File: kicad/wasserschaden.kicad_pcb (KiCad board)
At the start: 2 copper layers, 50.8 x 50.2 mm, 16 parts, among them J1 valve out, J2 12V in, U2 WeMos_mini

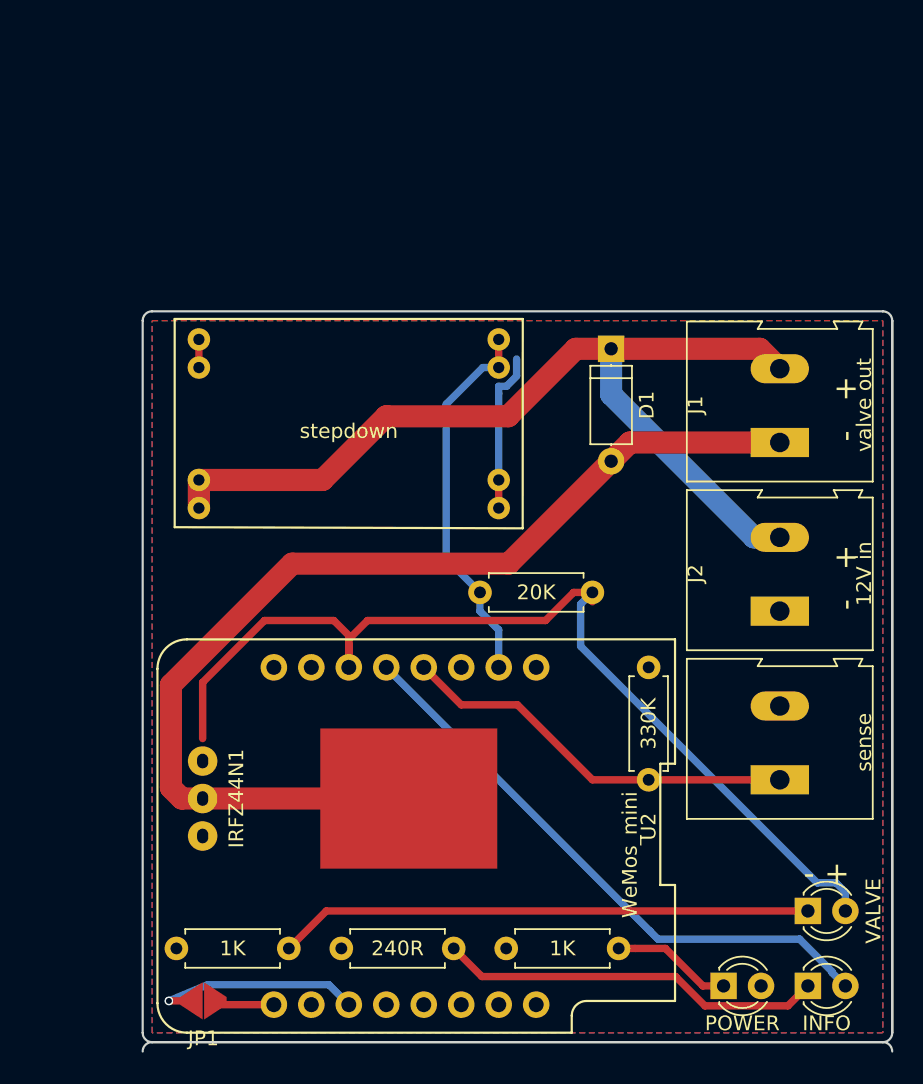
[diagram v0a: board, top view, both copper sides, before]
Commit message: major pcb rearangement
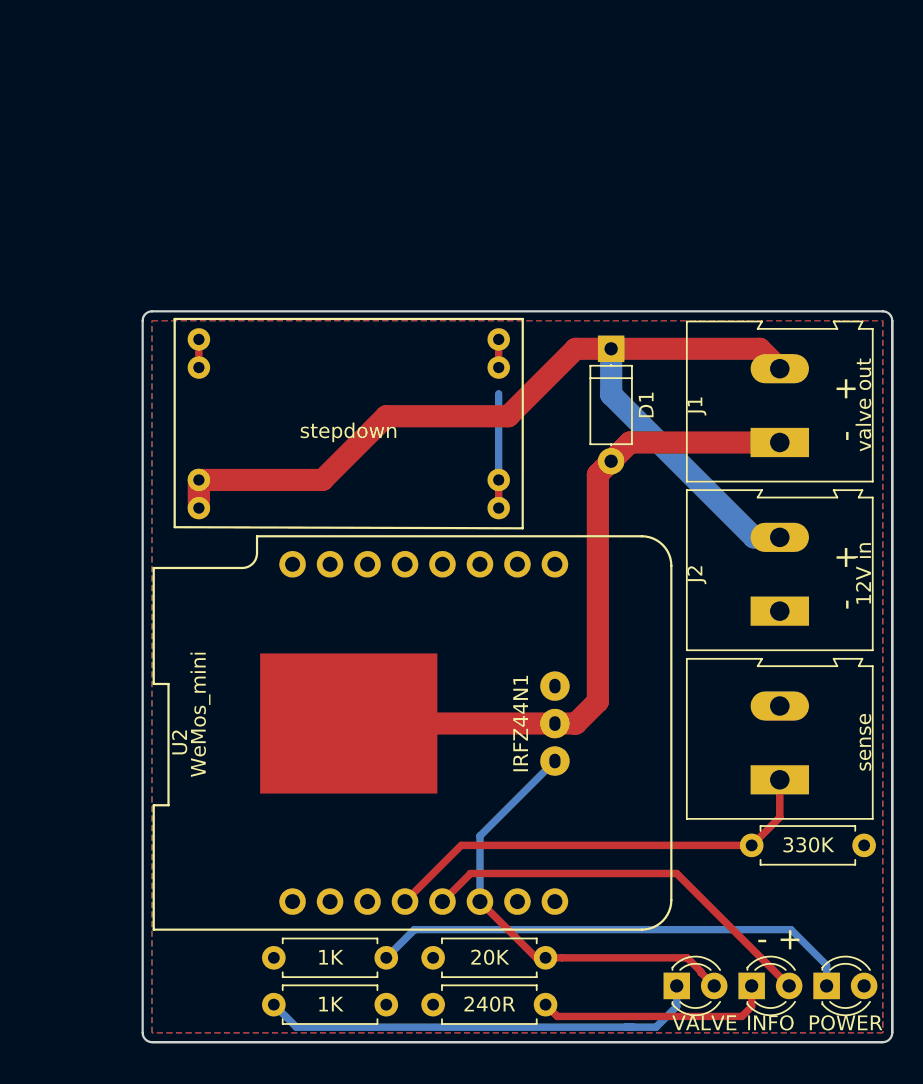
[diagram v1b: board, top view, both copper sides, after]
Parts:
- removed JP1: deepsleep jumper, custom:jumper
- moved 20K 25.0 mm to (145.4, 102.2)
- moved 1K 15.8 mm to (142.2, 102.2)
- moved 1K 14.7 mm to (142.2, 105.4), turned to 180 degrees
- moved IRFZ44N1 14.2 mm to (148.3, 86.4), turned to 0 degrees
- moved VALVE 10.2 mm to (161.9, 104.1)
- moved 330K 8.28 mm to (167.0, 94.6), turned to 0 degrees
- moved 240R 7.30 mm to (145.4, 105.4)
- moved U2 7.10 mm to (144.8, 87.0), turned to 0 degrees
- moved POWER 6.99 mm to (172.1, 104.1)
- moved INFO 3.81 mm to (167.0, 104.1)
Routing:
- net Net-(D2-Pad2): track 68.3 -> 30.5 mm
- net Net-(D1-Pad2): track 71.5 -> 46.1 mm
- net Net-(D3-Pad1): track 8.16 -> 33.0 mm
- net GND: track 27.7 -> 3.81 mm
- net Net-(JP1-Pad1): track 14.5 -> 0.00 mm, vias 1 -> 0
- net Net-(D4-Pad2): track 40.1 -> 27.4 mm
- net Net-(D4-Pad1): track 26.2 -> 16.0 mm
- net Net-(D2-Pad1): track 36.2 -> 30.4 mm
- net Net-(JP1-Pad2): track 4.07 -> 0.00 mm
- net +3V3: track 10.9 -> 7.75 mm
- net Net-(J3-Pad1): track 27.3 -> 30.3 mm
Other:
- board size 50.8 x 50.2 mm -> 50.8 x 49.5 mm

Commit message: pcb redesigen
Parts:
- added JP1: deepsleep jumper, custom:jumper, F.Cu at (151.1, 80.0)
- renumbered VALVE to D2, POWER to D3, INFO to D4, sense to J3, 20K to R1, 1K to R2, 1K to R3, 240R to R4, 330K to R5, stepdown to U1
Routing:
- net Net-(JP1-Pad1): track 0.00 -> 5.16 mm
- net Net-(JP1-Pad2): track 0.00 -> 5.16 mm
- added copper zone on F.Cu, net +3V3
- added copper zone on B.Cu, net GND
- removed copper zone on B.Cu, net +3V3
- removed copper zone on F.Cu, net GND
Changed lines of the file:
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@@
     (thickness 1.6)
     (drawings 13)
-    (tracks 54)
+    (tracks 58)
     (zones 0)
-    (modules 15)
+    (modules 16)
     (nets 22)
   )
@@
     (visible_elements FFFFFFFF)
     (pcbplotparams
-      (layerselection 0x010f0_80000001)
+      (layerselection 0x010f0_ffffffff)
       (usegerberextensions false)
       (usegerberattributes false)
@@
   (module custom:stepdown (layer F.Cu)
     (at 139.7 66.04)
-    (fp_text reference stepdown (at 0 0.5) (layer F.SilkS)
+    (fp_text reference U1 (at 0 0.5) (layer F.SilkS)
       (effects (font (size 1 1) (thickness 0.15)))
     )
@@
     (descr "Resistor, Axial_DIN0207 series, Axial, Horizontal, pin pitch=7.62mm, 0.25W = 1/4W, length*diameter=6.3*2.5mm^2, http://cdn-reichelt.de/documents/datenblatt/B400/1_4W%23YAG.pdf")
     (tags "Resistor Axial_DIN0207 series Axial Horizontal pin pitch 7.62mm 0.25W = 1/4W length 6.3mm diameter 2.5mm")
-    (fp_text reference 1K (at 3.81 0) (layer F.SilkS)
+    (fp_text reference R3 (at 3.81 0) (layer F.SilkS)
       (effects (font (size 1 1) (thickness 0.15)))
     )
@@
     (descr "LED, diameter 3.0mm, 2 pins")
     (tags "LED diameter 3.0mm 2 pins")
-    (fp_text reference INFO (at 1.27 2.54) (layer F.SilkS)
+    (fp_text reference D4 (at 1.27 2.54) (layer F.SilkS)
       (effects (font (size 1 1) (thickness 0.15)))
     )
@@
     (descr "LED, diameter 3.0mm, 2 pins")
     (tags "LED diameter 3.0mm 2 pins")
-    (fp_text reference POWER (at 1.27 2.54) (layer F.SilkS)
+    (fp_text reference D3 (at 1.27 2.54) (layer F.SilkS)
       (effects (font (size 1 1) (thickness 0.15)))
     )
@@
     (descr "LED, diameter 3.0mm, 2 pins")
     (tags "LED diameter 3.0mm 2 pins")
-    (fp_text reference VALVE (at 1.905 2.54 180) (layer F.SilkS)
+    (fp_text reference D2 (at 1.905 2.54 180) (layer F.SilkS)
       (effects (font (size 1 1) (thickness 0.15)))
     )
@@
     (descr "Resistor, Axial_DIN0207 series, Axial, Horizontal, pin pitch=7.62mm, 0.25W = 1/4W, length*diameter=6.3*2.5mm^2, http://cdn-reichelt.de/documents/datenblatt/B400/1_4W%23YAG.pdf")
     (tags "Resistor Axial_DIN0207 series Axial Horizontal pin pitch 7.62mm 0.25W = 1/4W length 6.3mm diameter 2.5mm")
-    (fp_text reference 20K (at 3.81 0) (layer F.SilkS)
+    (fp_text reference R1 (at 3.81 0) (layer F.SilkS)
       (effects (font (size 1 1) (thickness 0.15)))
     )
@@
     (descr "Resistor, Axial_DIN0207 series, Axial, Horizontal, pin pitch=7.62mm, 0.25W = 1/4W, length*diameter=6.3*2.5mm^2, http://cdn-reichelt.de/documents/datenblatt/B400/1_4W%23YAG.pdf")
     (tags "Resistor Axial_DIN0207 series Axial Horizontal pin pitch 7.62mm 0.25W = 1/4W length 6.3mm diameter 2.5mm")
-    (fp_text reference 1K (at 3.81 0 180) (layer F.SilkS)
+    (fp_text reference R2 (at 3.81 0 180) (layer F.SilkS)
       (effects (font (size 1 1) (thickness 0.15)))
     )
@@
     (descr "Resistor, Axial_DIN0207 series, Axial, Horizontal, pin pitch=7.62mm, 0.25W = 1/4W, length*diameter=6.3*2.5mm^2, http://cdn-reichelt.de/documents/datenblatt/B400/1_4W%23YAG.pdf")
     (tags "Resistor Axial_DIN0207 series Axial Horizontal pin pitch 7.62mm 0.25W = 1/4W length 6.3mm diameter 2.5mm")
-    (fp_text reference 240R (at 3.81 0) (layer F.SilkS)
+    (fp_text reference R4 (at 3.81 0) (layer F.SilkS)
       (effects (font (size 1 1) (thickness 0.15)))
     )
@@
     (descr "Altech AK300 terminal block, pitch 5.0mm, 45 degree angled, see http://www.mouser.com/ds/2/16/PCBMETRC-24178.pdf")
     (tags "Altech AK300 terminal block pitch 5.0mm")
-    (fp_text reference sense (at 2.54 5.715 90) (layer F.SilkS)
+    (fp_text reference J3 (at 2.54 5.715 90) (layer F.SilkS)
       (effects (font (size 1 1) (thickness 0.15)))
     )
@@
     (descr "Resistor, Axial_DIN0207 series, Axial, Horizontal, pin pitch=7.62mm, 0.25W = 1/4W, length*diameter=6.3*2.5mm^2, http://cdn-reichelt.de/documents/datenblatt/B400/1_4W%23YAG.pdf")
     (tags "Resistor Axial_DIN0207 series Axial Horizontal pin pitch 7.62mm 0.25W = 1/4W length 6.3mm diameter 2.5mm")
-    (fp_text reference 330K (at 3.81 0 180) (layer F.SilkS)
+    (fp_text reference R5 (at 3.81 0 180) (layer F.SilkS)
       (effects (font (size 1 1) (thickness 0.15)))
     )
@@
     )
   )
+  (module custom:jumper (layer F.Cu)
+    (at 151.13 80.01)
+    (fp_text reference JP1 (at 0 2.54) (layer F.SilkS)
+      (effects (font (size 1 1) (thickness 0.15)))
+    )
+    (fp_text value "deepsleep jumper" (at 0 1.27) (layer F.Fab)
+      (effects (font (size 1 1) (thickness 0.15)))
+    )
+    (pad 1 smd trapezoid (at -0.8128 0) (size 1.524 1.524) (rect_delta -1 0 ) (layers F.Cu F.Paste F.Mask)
+      (net 19 "Net-(JP1-Pad1)"))
+    (pad 2 smd trapezoid (at 0.8128 0) (size 1.524 1.524) (rect_delta 1 0 ) (layers F.Cu F.Paste F.Mask)
+      (net 20 "Net-(JP1-Pad2)"))
+  )
   (gr_arc (start 175.895 107.315) (end 176.53 107.315) (angle 90) (layer Edge.Cuts) (width 0.15))
   (gr_text "- +" (at 168.91 100.965) (layer F.SilkS)
@@
   (segment (start 149.86 69.85) (end 149.86 71.755) (width 0.5) (layer F.Cu) (net 18))
   (segment (start 149.86 69.85) (end 149.86 64.008) (width 0.5) (layer B.Cu) (net 18))
+  (segment (start 148.59 75.565) (end 148.59 78.2828) (width 0.5) (layer F.Cu) (net 19))
+  (segment (start 150.3172 80.01) (end 148.59 78.2828) (width 0.5) (layer F.Cu) (net 19))
+  (segment (start 153.67 78.2828) (end 153.67 75.565) (width 0.5) (layer F.Cu) (net 20))
+  (segment (start 151.9428 80.01) (end 153.67 78.2828) (width 0.5) (layer F.Cu) (net 20))
   (segment (start 147.32 94.615) (end 167.005 94.615) (width 0.5) (layer F.Cu) (net 21))
   (segment (start 143.51 98.425) (end 147.32 94.615) (width 0.5) (layer F.Cu) (net 21))
   (segment (start 168.91 92.71) (end 167.005 94.615) (width 0.5) (layer F.Cu) (net 21))
   (segment (start 168.91 90.17) (end 168.91 92.71) (width 0.5) (layer F.Cu) (net 21))
-  (zone (net 3) (net_name GND) (layer F.Cu) (hatch edge 0.508)
+  (zone (net 18) (net_name +3V3) (layer F.Cu) (hatch edge 0.508)
     (connect_pads (clearance 0.508))
     (min_thickness 0.254)
@@
     )
   )
-  (zone (net 18) (net_name +3V3) (layer B.Cu) (hatch edge 0.508)
+  (zone (net 3) (net_name GND) (layer B.Cu) (hatch edge 0.508)
     (connect_pads (clearance 0.508))
     (min_thickness 0.254)

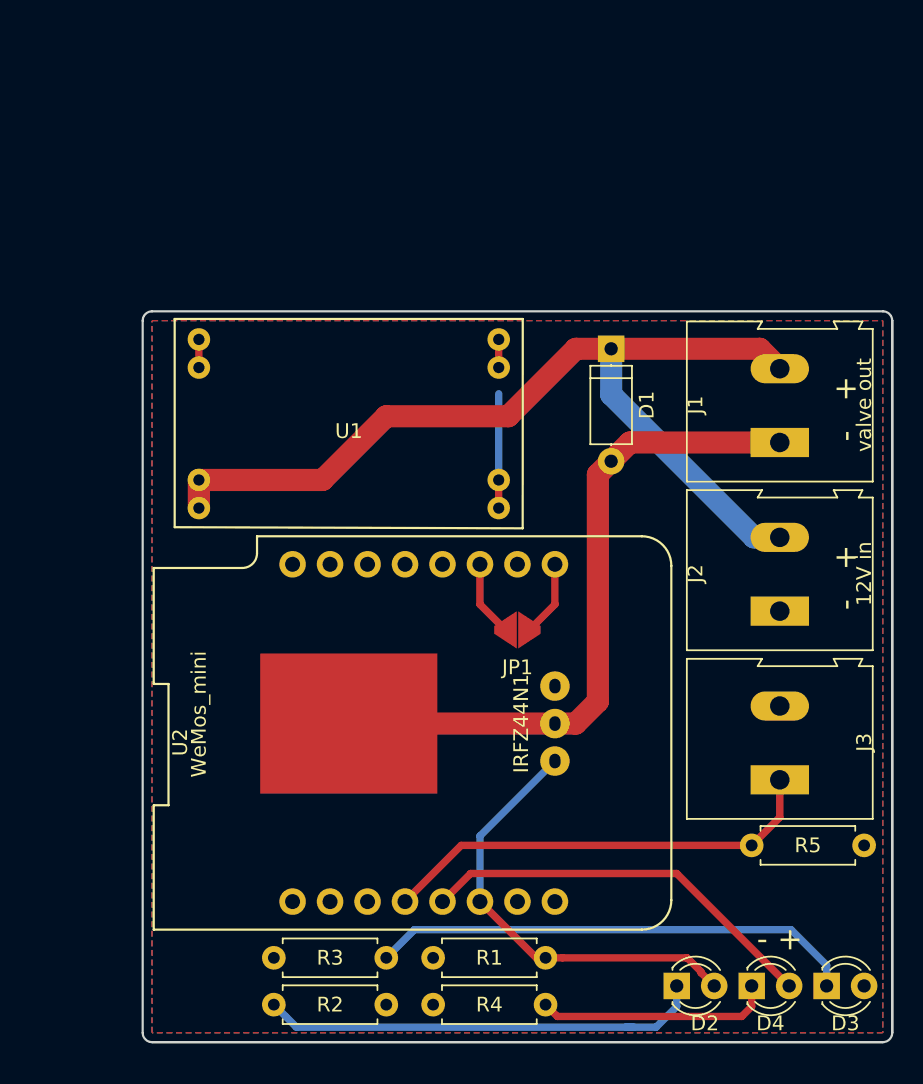
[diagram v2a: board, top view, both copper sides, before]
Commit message: added temperature sensor
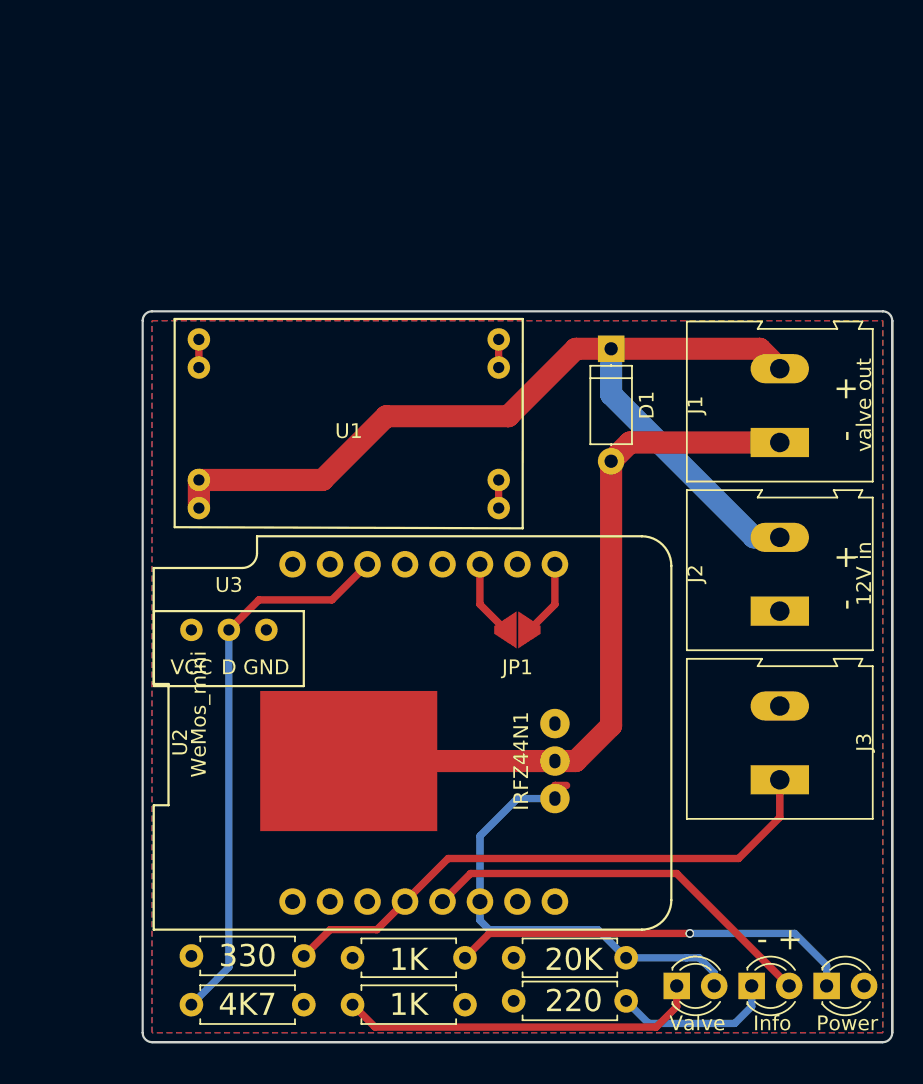
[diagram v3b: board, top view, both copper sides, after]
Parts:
- added R6: R, Resistors_THT:R_Axial_DIN0207_L6.3mm_D2.5mm_P7.62mm_Horizontal, F.Cu at (136.7, 105.4)
- added U3: DS18B20, custom:temperature_sensor, F.Cu at (131.6, 77.5)
- moved R5 31.3 mm to (136.7, 102.1), turned to 180 degrees
- moved R4 5.47 mm to (150.9, 105.2)
- moved R1 5.46 mm to (150.9, 102.2)
- moved R2 5.33 mm to (147.6, 105.4)
- moved R3 5.33 mm to (147.6, 102.2)
- moved IRFZ44N1 2.54 mm to (148.3, 88.9)
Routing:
- net Net-(R6-Pad2): track 0.00 -> 37.7 mm
- net Net-(J3-Pad1): track 30.3 -> 38.7 mm
- net +3V3: track 7.75 -> 1.91 mm
- net Net-(D2-Pad1): track 30.4 -> 24.6 mm
- net Net-(D3-Pad1): track 33.0 -> 27.5 mm, vias 0 -> 1
- net Net-(D4-Pad1): track 16.0 -> 11.0 mm
- net Net-(D1-Pad2): track 46.1 -> 48.7 mm
- net Net-(D2-Pad2): track 30.5 -> 32.4 mm
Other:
- board text added: "1K"
- board text added: "20K"
- board text added: "220"
- board text added: "330"
- board text added: "4K7"
- board text added: "Info"
- board text added: "Power"
- board text added: "Valve"

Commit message: added R values, improved stepdown footprint, rerouted resistors
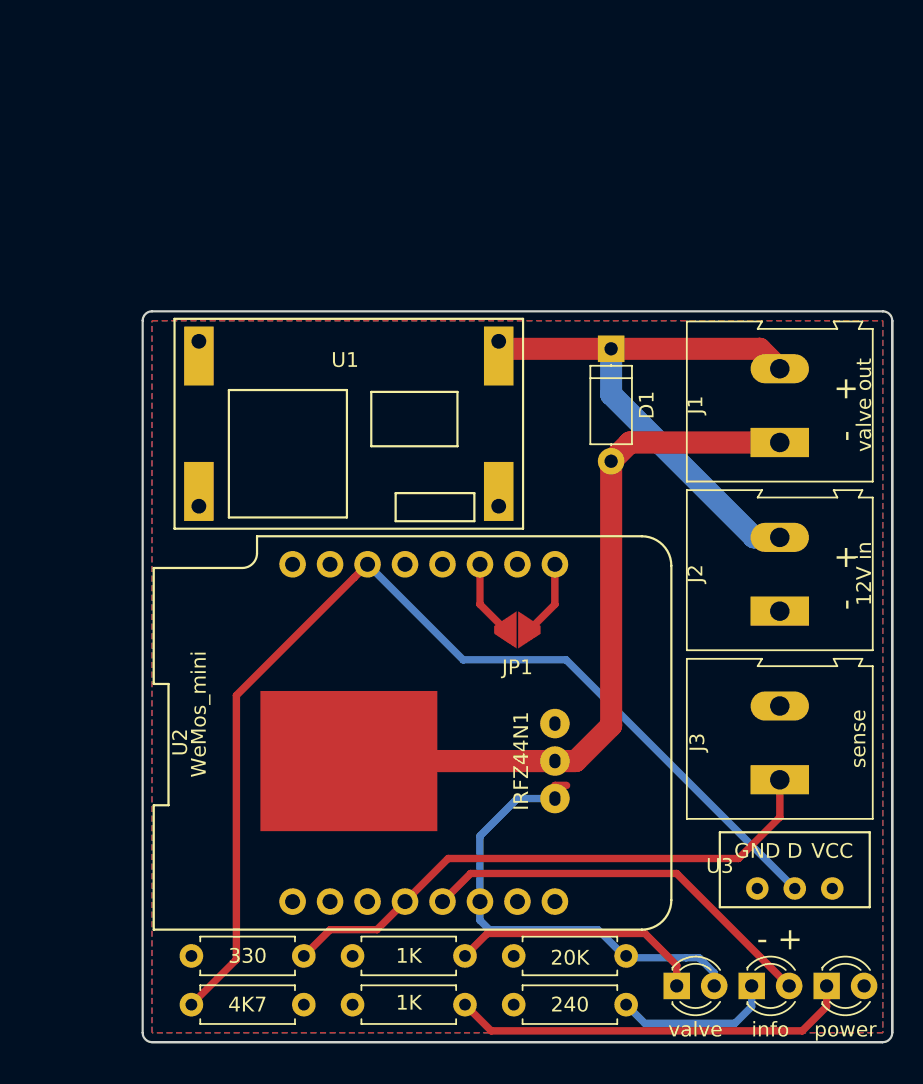
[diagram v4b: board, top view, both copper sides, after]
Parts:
- D2: value LED -> valve
- D3: value LED -> power
- D4: value LED -> info
- JP1: value deepsleep jumper -> deepsleep
- R2, R3: value R -> 1K
- R4: value R -> 240
- R5: value R -> 330
- R6: value R -> 4K7
- moved U3 44.5 mm to (169.9, 100.1), turned to 0 degrees
- moved R2 8.30 mm to (140.0, 102.1), turned to 0 degrees
- moved R3 3.17 mm to (147.6, 105.4)
- moved R4 0.25 mm to (150.9, 105.4)
- moved R1 0.13 mm to (150.9, 102.1)
- turned U1 to 180 degrees
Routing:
- net Net-(R6-Pad2): track 37.7 -> 72.8 mm
- net +12V: track 64.1 -> 40.3 mm
- net Net-(D2-Pad1): track 24.6 -> 17.3 mm
- net Net-(D3-Pad1): track 27.5 -> 27.3 mm, vias 1 -> 0
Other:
- board text removed: "1K"
- board text removed: "20K"
- board text removed: "220"
- board text removed: "330"
- board text removed: "4K7"
- board text removed: "Info"
- board text removed: "Power"
- board text removed: "Valve"

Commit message: nicer silkscreen
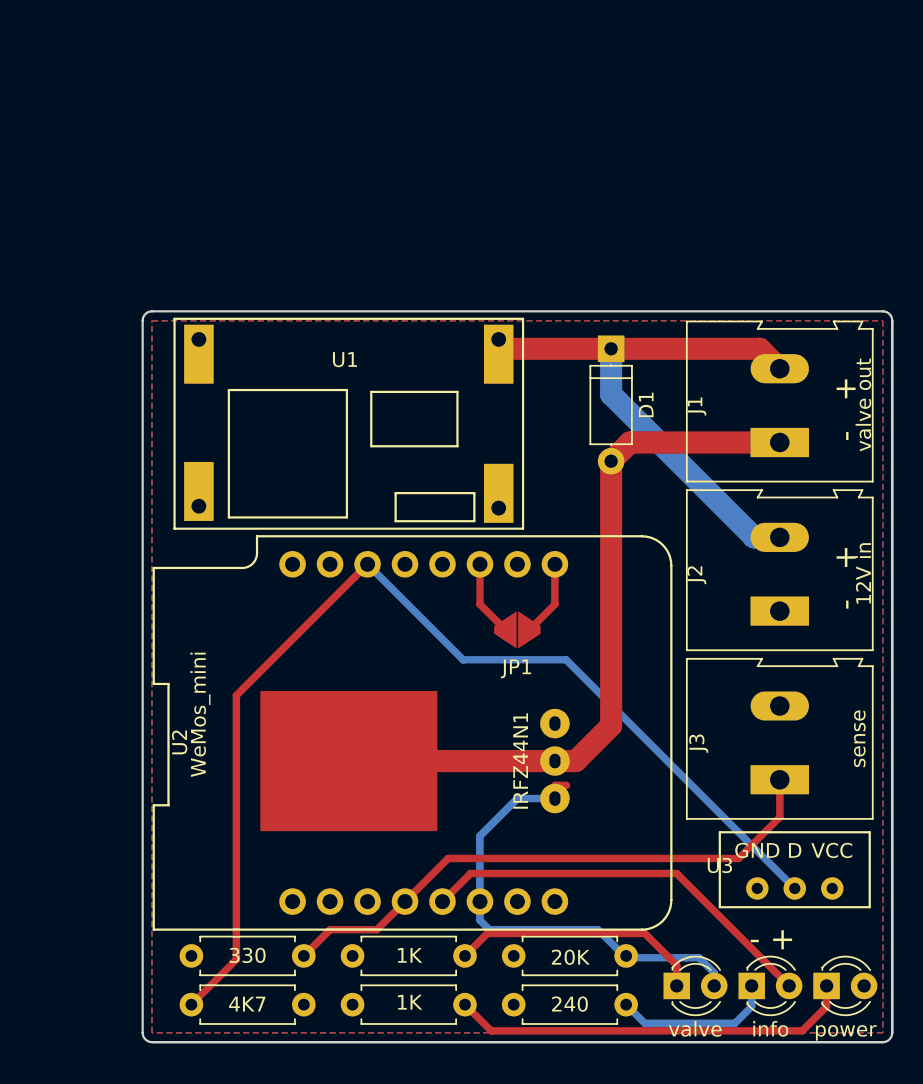
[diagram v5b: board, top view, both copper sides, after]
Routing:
- net +12V: track 40.3 -> 41.0 mm
